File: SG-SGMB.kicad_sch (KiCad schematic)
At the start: 0 parts

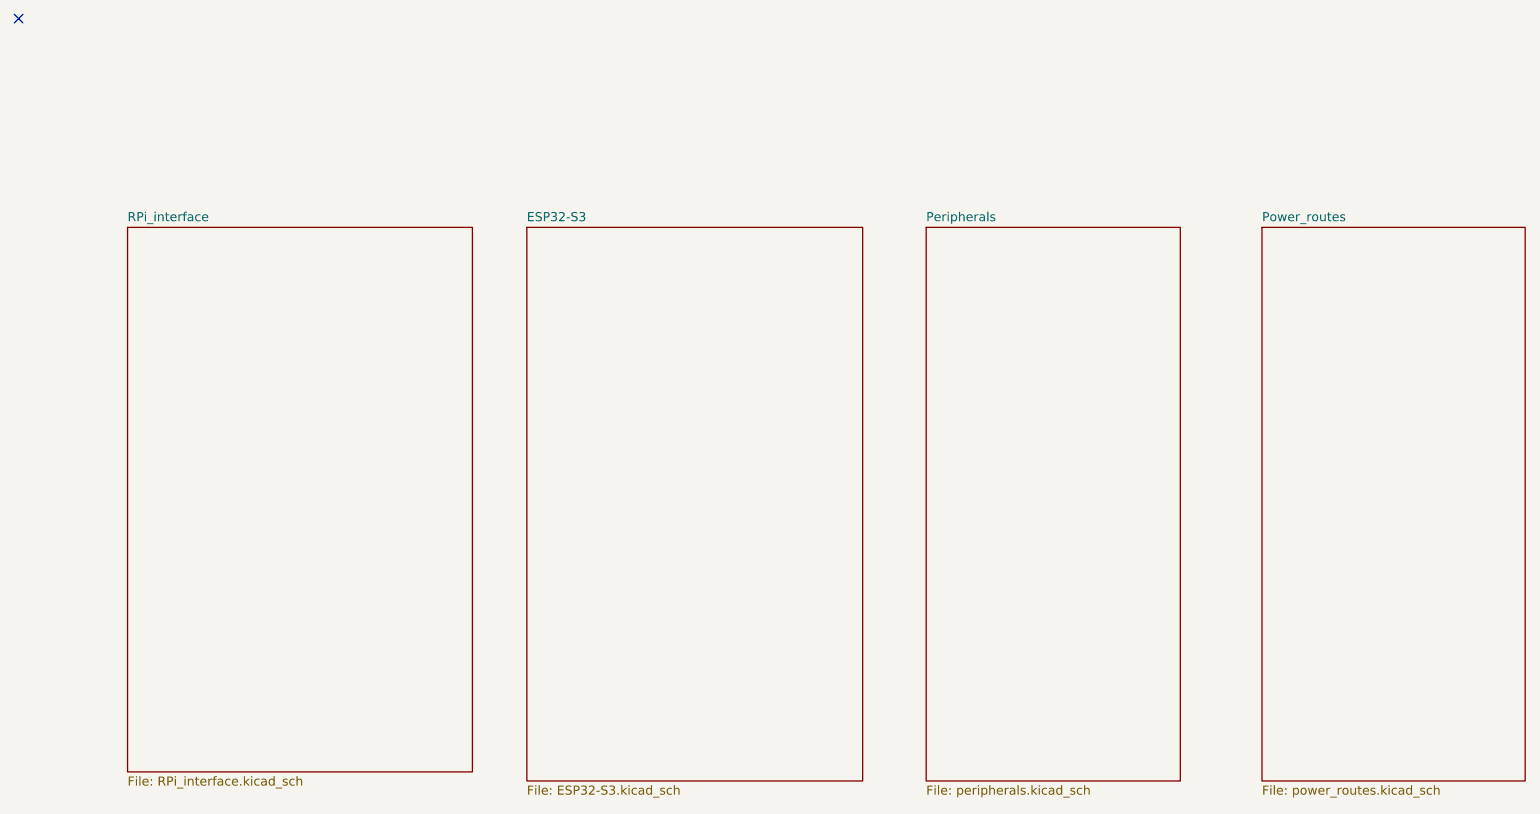
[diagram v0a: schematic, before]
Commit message: feat(power & programmer): Finished Schematic building. Now sourcing for parts.
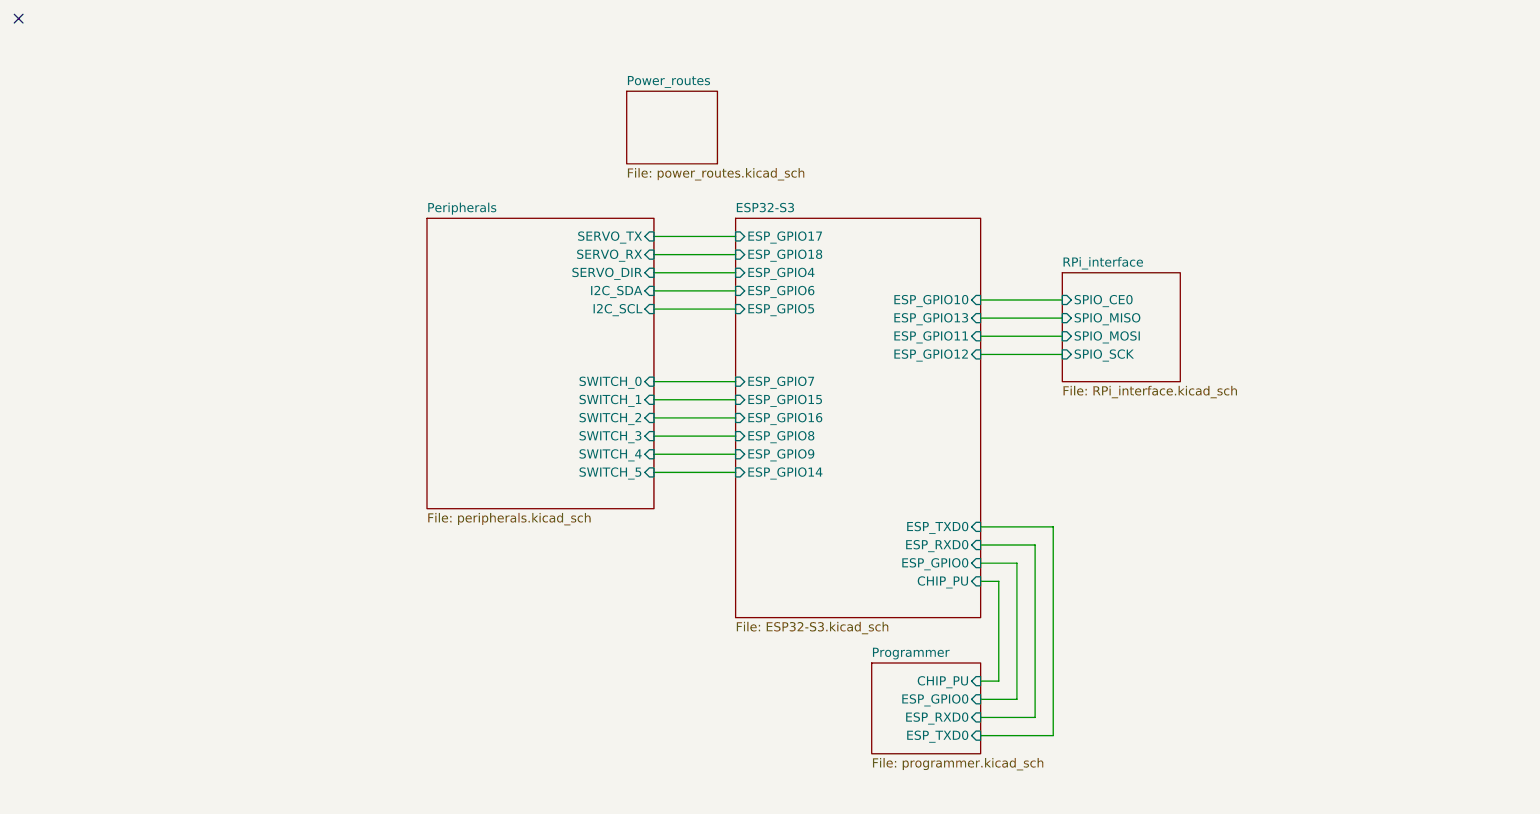
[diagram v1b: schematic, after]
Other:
- added sheet Programmer (programmer.kicad_sch)
- sheet ESP32-S3 ports: added CHIP_PU, ESP_GPIO0, ESP_GPIO10, ESP_GPIO11, ESP_GPIO12, ESP_GPIO13, ESP_GPIO14, ESP_GPIO15, ESP_GPIO16, ESP_GPIO17, ESP_GPIO18, ESP_GPIO4, ESP_GPIO5, ESP_GPIO6, ESP_GPIO7, ESP_GPIO8, ESP_GPIO9, ESP_RXD0, ESP_TXD0; removed none
- sheet Peripherals ports: added I2C_SCL, I2C_SDA, SERVO_DIR, SERVO_RX, SERVO_TX, SWITCH_0, SWITCH_1, SWITCH_2, SWITCH_3, SWITCH_4, SWITCH_5; removed none
- sheet RPi_interface ports: added SPIO_CE0, SPIO_MISO, SPIO_MOSI, SPIO_SCK; removed none
